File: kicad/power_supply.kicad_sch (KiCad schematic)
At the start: 13 parts, among them T1 reuse / AnTek AS-0524, U1 LM317T

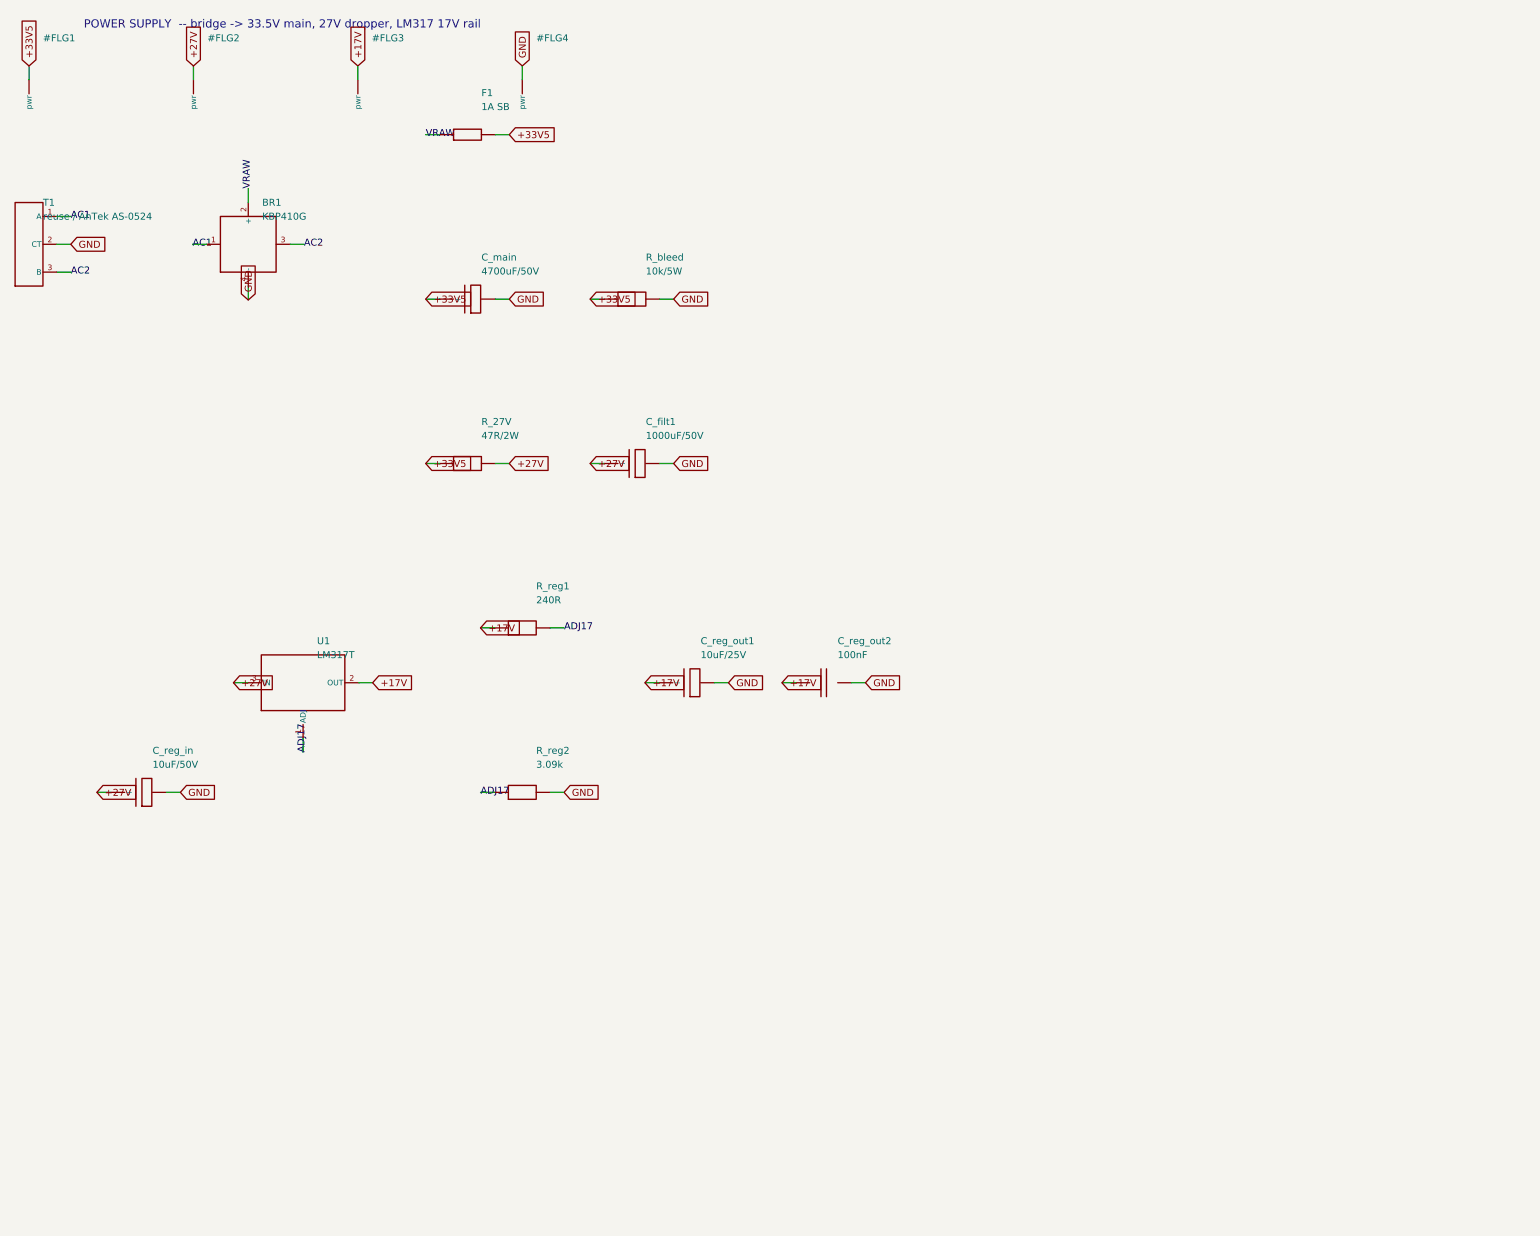
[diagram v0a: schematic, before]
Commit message: Schematic passes KiCad 8 ERC (0 violations); add op-amp mid-rail bias
Installed KiCad 8.0.9 and ran a real Electrical Rules Check on the generated
hierarchy. Drove it to 0 violations:
- snapped every pin/wire endpoint to the 1.27 mm connection grid (was 338
  endpoint_off_grid violations)
- gave the footswitch lines FS_REV/FS_TREM/FS_MRB a real second endpoint via
  100k control pulldowns on the reverb/tremolo/mrb sheets (was 3 dangling labels)

Also made the single-supply TL072 stages electrically real: added a mid-rail
VBIAS network (R_vb1/R_vb2 + C_vb on the Power Supply sheet) and referenced the
reverb driver and tremolo LFO inputs/gain-returns to VBIAS instead of GND
(design addition, flagged in the sheet notes).

Result: kicad-cli 8.0.9 sch erc -> 0 violations; netlist 102 components, 58
nets, 0 unconnected pins; VBIAS spans 10 nodes. Updated SCHEMATIC-BUILD.md,
kicad/README.md, CHANGELOG.md.

https://claude.ai/code/session_01PkrfUi9tvZfLvudJ7h23qD
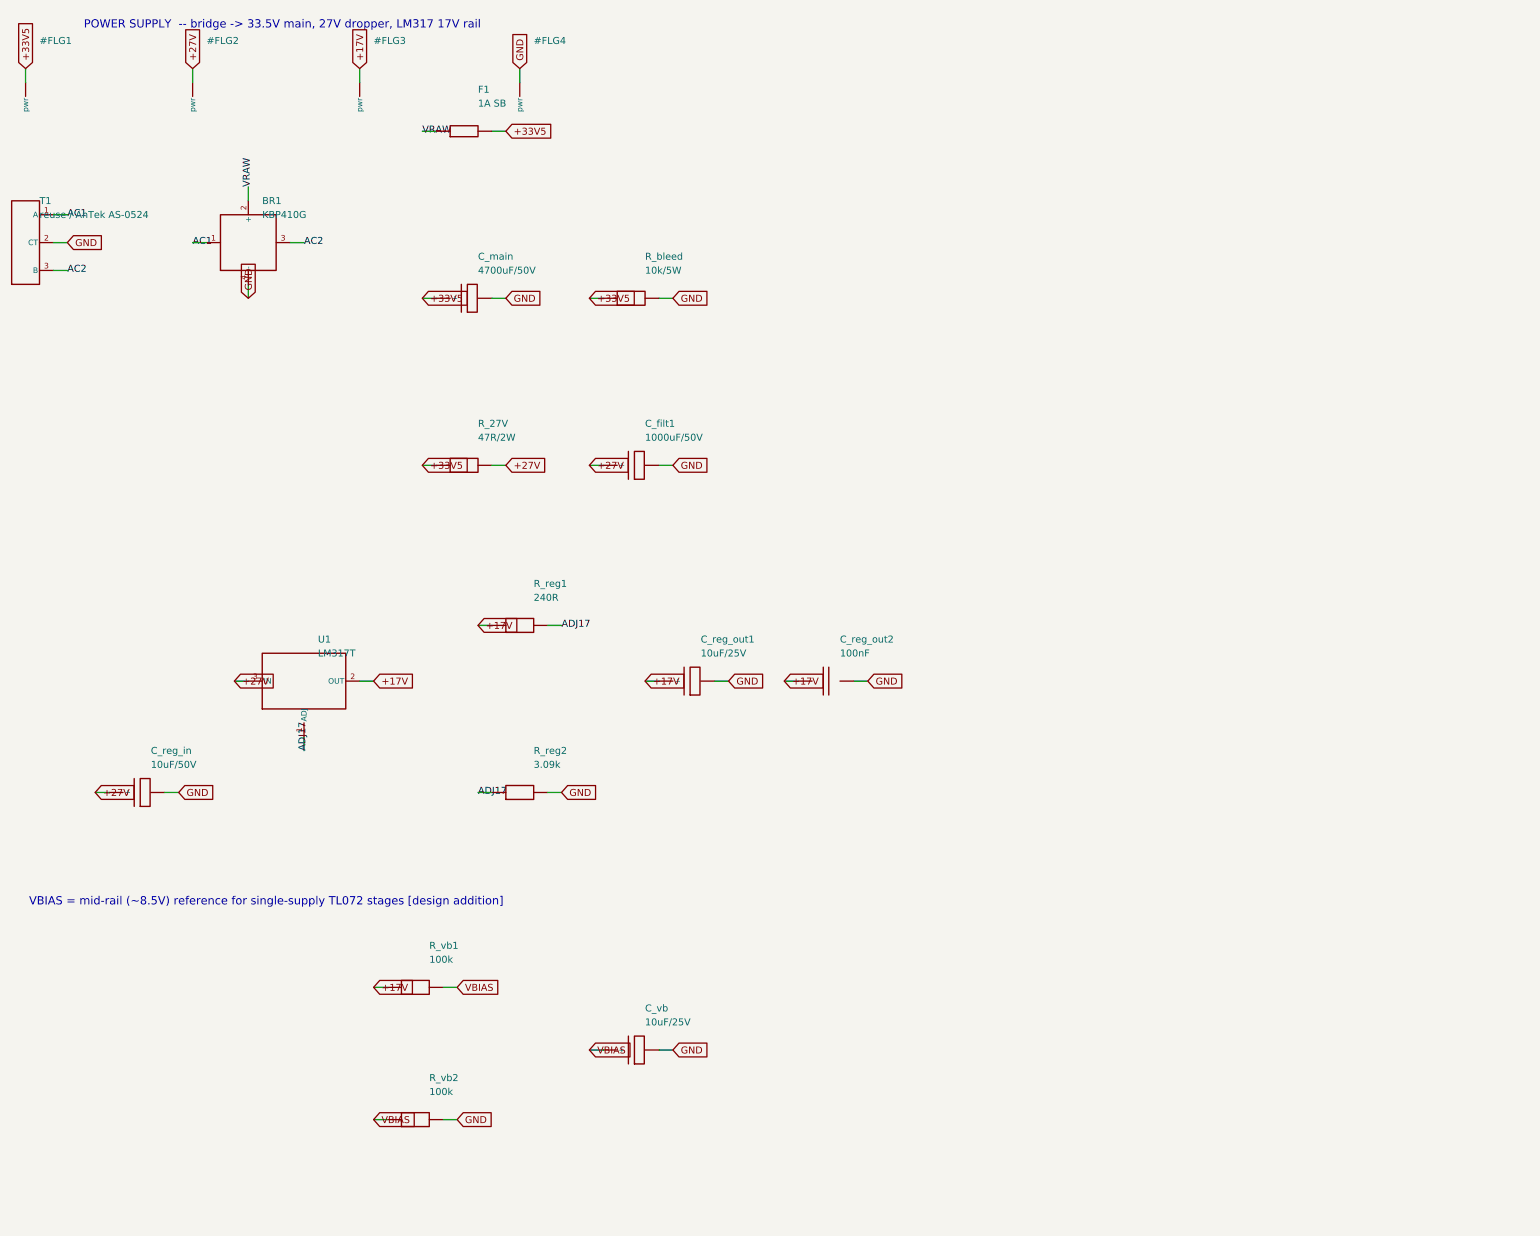
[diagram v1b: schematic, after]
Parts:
- added C_vb: 10uF/25V, symbol cr_primitives:CP
- added R_vb1, R_vb2: 100k, symbol cr_primitives:R
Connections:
- net +17V: now also R_vb1.1
- net GND: now also C_vb.2, R_vb2.2
- new net VBIAS: C_vb.1 (+), R_vb1.2, R_vb2.1
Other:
- note added: "VBIAS = mid-rail (~8.5V) reference for single-supply TL072 stages [design addition]"

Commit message: Generate auto-placed PCB (102 footprints, GND pour, board outline)
Build cambridge_reverb.kicad_pcb from the schematic via kicad/gen/gen_pcb.py
(KiCad 8 pcbnew API): assign a THT footprint to every component (standard libs
for generics + the project footprints for VTL5C1 and the 1H toroid), place all
102 footprints (off-board connectors on a bottom wiring-edge strip, toroid in a
reserved spot), assign all 58 nets to pads, draw a 190x115 mm Edge.Cuts outline,
and pour a bottom-layer GND plane. Footprint assignments also carry into the
schematic symbols.

The board opens in KiCad and the ratsnest matches the ERC-clean schematic. It is
placed but NOT routed: kicad-cli pcb drc is dominated by 130 unconnected
(unrouted signal nets; GND is poured) plus cosmetic silk/courtyard overlaps from
dense auto-placement at chassis size -- documented in kicad/PCB-NOTES.md with the
remaining hand-work (placement into floor-plan zones, routing, DRC-to-zero,
Gerbers). Net classes (Default/Power/HighCurrent) carry over for routing.

Also: schematic resistor footprint switched to the compact vertical variant;
gitignore DRC/ERC .rpt reports.

https://claude.ai/code/session_01PkrfUi9tvZfLvudJ7h23qD
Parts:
- BR1: footprint (none) -> Connector_PinHeader_2.54mm:PinHeader_1x04_P2.54mm_Vertical
- C_filt1, C_main, C_reg_in, C_reg_out1, C_vb: footprint (none) -> Capacitor_THT:CP_Radial_D8.0mm_P3.50mm
- C_reg_out2: footprint (none) -> Capacitor_THT:C_Disc_D7.5mm_W2.5mm_P5.00mm
- F1: footprint (none) -> Fuse:Fuseholder_Clip-5x20mm_Eaton_1A5601-01_Inline_P20.80x6.76mm_D1.70mm_Horizontal
- R_27V, R_bleed, R_reg1, R_reg2, R_vb1, R_vb2: footprint (none) -> Resistor_THT:R_Axial_DIN0207_L6.3mm_D2.5mm_P5.08mm_Vertical
- T1: footprint (none) -> Connector_PinHeader_2.54mm:PinHeader_1x03_P2.54mm_Vertical
- U1: footprint (none) -> Package_TO_SOT_THT:TO-220-3_Vertical

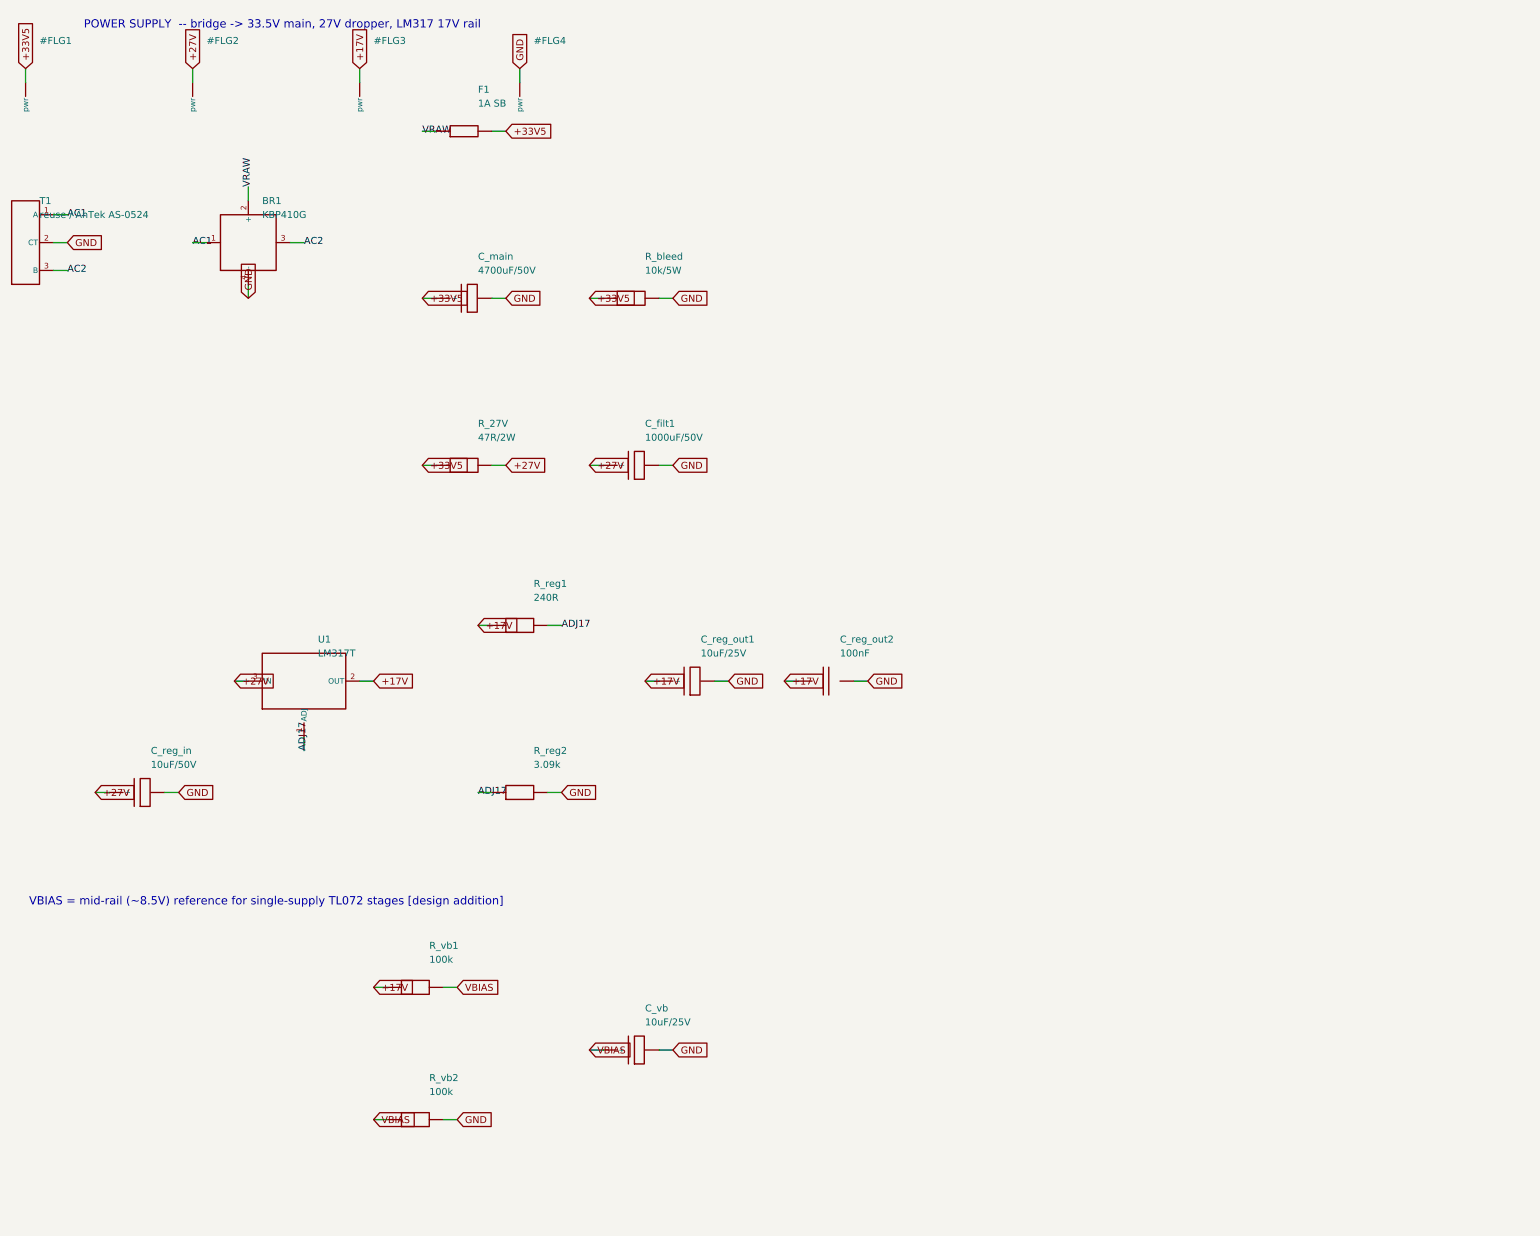
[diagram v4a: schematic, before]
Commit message: Audit pass: center schematic pages, PCB layout audit, SPICE audit
Schematic: gen_kicad.py now defers draw-op emission, computes each sheet's
content bounding box, and translates it to the page center (grid-snapped so pins
stay on the 1.27mm grid). All 8 sheets are centered on the page instead of
crammed top-left; ERC still 0 violations.

PCB: full category-by-category audit in kicad/PCB-AUDIT.md (footprints,
placement, net classes, copper/GND, routing) with prioritized fixes. Applied:
- the 5 reused/off-board pots were modeled with a 16mm panel-pot footprint; they
  are panel-mounted (wired off-board), so they're now 3-pad wiring connectors --
  more correct and a big silk-overlap source removed (packing 51%->48%)
- centered the component grid
Documented findings: LM1875 TO-220-5 annular is 0.0875mm (1.275mm pad on 1.1mm
drill) vs the 0.15mm rule; KBP410G bridge uses a placeholder header footprint;
silk/courtyard overlaps are a density symptom (the 82% packing on the 155x90
safe-bet). Non-routing DRC errors: 9; demo board still 0.

SPICE: audited every netlist/model (spice/README.md). All five run under
ngspice-42 (exit 0) and match the documented numbers; no correctness issues.

https://claude.ai/code/session_01PkrfUi9tvZfLvudJ7h23qD
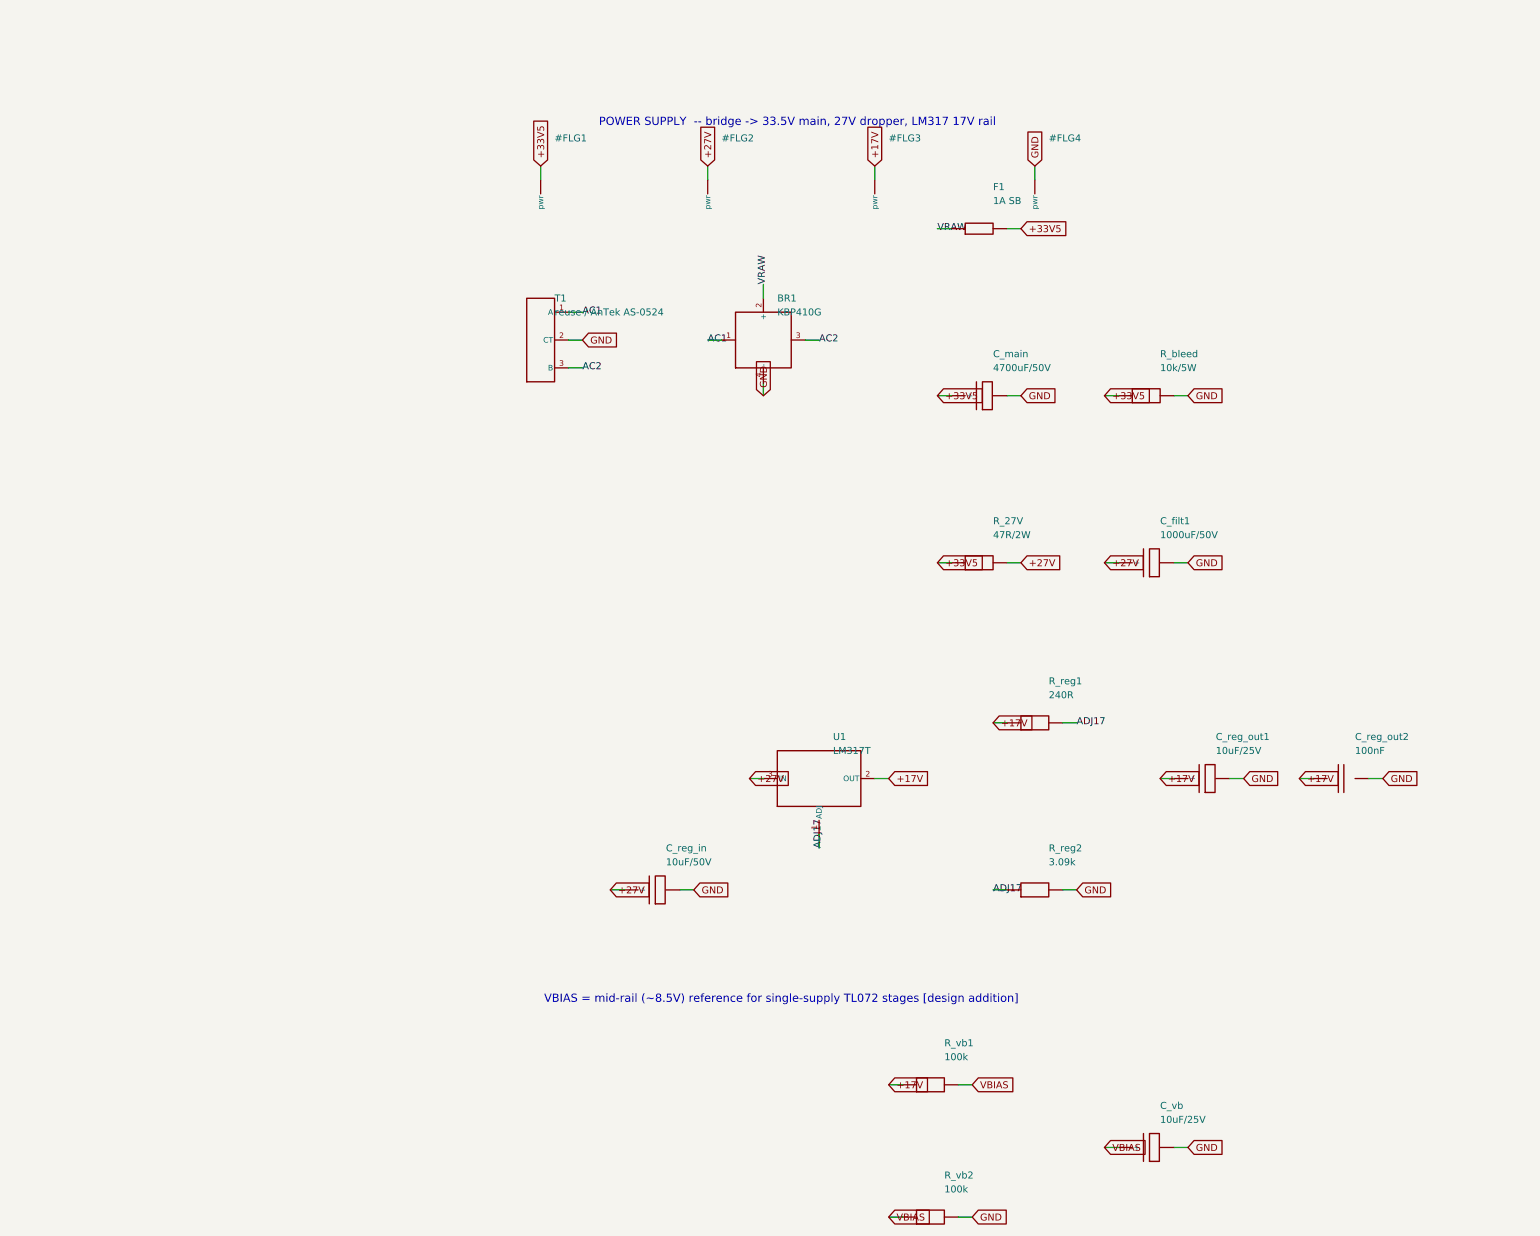
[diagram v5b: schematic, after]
